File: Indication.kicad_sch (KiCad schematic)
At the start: 29 parts

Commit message: Убрал питание 3.3В
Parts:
- removed C10, C11, C12, C13, C14, C9: 56p, Capacitor_SMD:C_0805_2012Metric_Pad1.18x1.45mm_HandSolder, symbol Device:C_Small
- removed D11: FLT, LED_SMD:LED_0805_2012Metric_Pad1.15x1.40mm_HandSolder, symbol Device:LED_Small
- removed D12: RDY, LED_SMD:LED_0805_2012Metric_Pad1.15x1.40mm_HandSolder, symbol Device:LED_Small
- removed D13: SN74AC08DR, Package_SO:SOIC-14_3.9x8.7mm_P1.27mm, symbol Logic:SN74AC08DR
- removed R15: 10k, Resistor_SMD:R_0805_2012Metric_Pad1.20x1.40mm_HandSolder, symbol Device:R_Small
- removed R16, R18: 330, Resistor_SMD:R_0805_2012Metric_Pad1.20x1.40mm_HandSolder, symbol Device:R_Small
- removed R17, R19, R20, R21, R22: 120, Resistor_SMD:R_0805_2012Metric_Pad1.20x1.40mm_HandSolder, symbol Device:R_Small
- added D6: SN74AHC1G08DBVR, symbol Logic_My:SN74AHC1G08DBVR
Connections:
- net FLT_L1 is gone; now on net FLT: C7.1, D9.1 (K), R13.1
- net RDY_L1 is gone; now on net RDY: C8.1, R12.2, R14.1
- net FLT: now also D6.2 (A)
- net GND: now also D6.3 (GND)
- net RDY: now also D6.1 (B)
- net at D14.4 (DI): now also D6.4 (Y)
- net +3V3 renamed +5V
- net +5V: now also D6.5 (Vcc); no longer R13.2
- no-connect marks 4 -> 1
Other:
- moved on the sheet: C15

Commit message: Развел все дорожки
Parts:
- D6: footprint (none) -> Package_TO_SOT_SMD:SOT-23-5
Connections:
- net +5V: now also R13.2
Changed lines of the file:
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@@
-	)
-	(junction
-		(at 76.962 83.566)
-		(diameter 0)
-		(color 0 0 0 0)
 	)
 	(junction
@@
 		(color 0 0 0 0)
 	)
+	(junction
+		(at 76.835 83.82)
+		(diameter 0)
+		(color 0 0 0 0)
+	)
 	(no_connect
 		(at 221.996 95.758)
@@
 	(wire
 		(pts
+			(xy 76.835 83.185) (xy 76.835 83.82)
+		)
+		(stroke
+			(width 0)
+			(type default)
+		)
+	)
+	(wire
+		(pts
 			(xy 242.57 105.41) (xy 242.57 106.426)
 		)
@@
 	(wire
 		(pts
-			(xy 70.104 83.566) (xy 76.962 83.566)
+			(xy 69.977 83.82) (xy 76.835 83.82)
 		)
 		(stroke
@@
 	(wire
 		(pts
-			(xy 76.962 84.582) (xy 76.962 83.566)
+			(xy 76.835 84.836) (xy 76.835 83.82)
 		)
 		(stroke
@@
 	(global_label "FLT"
 		(shape input)
-		(at 70.104 83.566 180)
+		(at 69.977 83.82 180)
 		(fields_autoplaced yes)
 		(effects
@@
 		)
 		(property "Intersheetrefs" "${INTERSHEET_REFS}"
-			(at 64.0345 83.566 0)
+			(at 63.9075 83.82 0)
 			(effects
 				(font
@@
 	(symbol
 		(lib_id "power:+5V")
-		(at 76.962 78.232 0)
+		(at 76.835 78.105 0)
 		(unit 1)
 		(exclude_from_sim no)
@@
 		(dnp no)
 		(property "Reference" "#PWR017"
-			(at 76.962 82.042 0)
+			(at 76.835 81.915 0)
 			(effects
 				(font
@@
 		)
 		(property "Value" "+5V"
-			(at 76.962 74.676 0)
+			(at 76.835 74.549 0)
 			(effects
 				(font
@@
 		)
 		(property "Footprint" ""
-			(at 76.962 78.232 0)
+			(at 76.835 78.105 0)
 			(effects
 				(font
@@
 		)
 		(property "Datasheet" ""
-			(at 76.962 78.232 0)
+			(at 76.835 78.105 0)
 			(effects
 				(font
@@
 		)
 		(property "Description" "Power symbol creates a global label with name \"+5V\""
-			(at 76.962 78.232 0)
+			(at 76.835 78.105 0)
 			(effects
 				(font
@@
 			)
 		)
-		(property "Footprint" ""
+		(property "Footprint" "Package_TO_SOT_SMD:SOT-23-5"
 			(at 177.292 99.06 0)
 			(effects
@@
 	(symbol
 		(lib_id "power:GND")
-		(at 76.962 89.662 0)
+		(at 76.835 89.916 0)
 		(unit 1)
 		(exclude_from_sim no)
@@
 		(dnp no)
 		(property "Reference" "#PWR018"
-			(at 76.962 96.012 0)
+			(at 76.835 96.266 0)
 			(effects
 				(font
@@
 		)
 		(property "Value" "GND"
-			(at 74.93 93.726 0)
+			(at 74.803 93.98 0)
 			(effects
 				(font
@@
 		)
 		(property "Footprint" ""
-			(at 76.962 89.662 0)
+			(at 76.835 89.916 0)
 			(effects
 				(font
@@
 		)
 		(property "Datasheet" ""
-			(at 76.962 89.662 0)
+			(at 76.835 89.916 0)
 			(effects
 				(font
@@
 		)
 		(property "Description" ""
-			(at 76.962 89.662 0)
+			(at 76.835 89.916 0)
 			(effects
 				(font
@@
 	(symbol
 		(lib_id "Device:C_Small")
-		(at 76.962 87.122 0)
+		(at 76.835 87.376 0)
 		(unit 1)
 		(exclude_from_sim no)
@@
 		(dnp no)
 		(property "Reference" "C7"
-			(at 74.295 85.598 0)
+			(at 74.168 85.852 0)
 			(effects
 				(font
@@
 		)
 		(property "Value" "56p"
-			(at 73.279 88.773 0)
+			(at 73.152 89.027 0)
 			(effects
 				(font
@@
 		)
 		(property "Footprint" "Capacitor_SMD:C_0805_2012Metric_Pad1.18x1.45mm_HandSolder"
-			(at 76.962 87.122 0)
+			(at 76.835 87.376 0)
 			(effects
 				(font
@@
 		)
 		(property "Datasheet" "~"
-			(at 76.962 87.122 0)
+			(at 76.835 87.376 0)
 			(effects
 				(font
@@
 		)
 		(property "Description" ""
-			(at 76.962 87.122 0)
+			(at 76.835 87.376 0)
 			(effects
 				(font
@@
 	(symbol
 		(lib_id "Device:R_Small")
-		(at 76.962 81.026 180)
+		(at 76.835 80.645 180)
 		(unit 1)
 		(exclude_from_sim no)
@@
 		(dnp no)
 		(property "Reference" "R13"
-			(at 79.883 82.169 0)
+			(at 79.756 81.788 0)
 			(effects
 				(font
@@
 		)
 		(property "Value" "10k"
-			(at 79.883 80.391 0)
+			(at 79.756 80.01 0)
 			(effects
 				(font
@@
 		)
 		(property "Footprint" "Resistor_SMD:R_0805_2012Metric_Pad1.20x1.40mm_HandSolder"
-			(at 76.962 81.026 0)
+			(at 76.835 80.645 0)
 			(effects
 				(font
@@
 		)
 		(property "Datasheet" "~"
-			(at 76.962 81.026 0)
+			(at 76.835 80.645 0)
 			(effects
 				(font
@@
 		)
 		(property "Description" ""
-			(at 76.962 81.026 0)
-			(effects
-				(font
+			(at 76.835 80.645 0)
+			(effects
+				(font

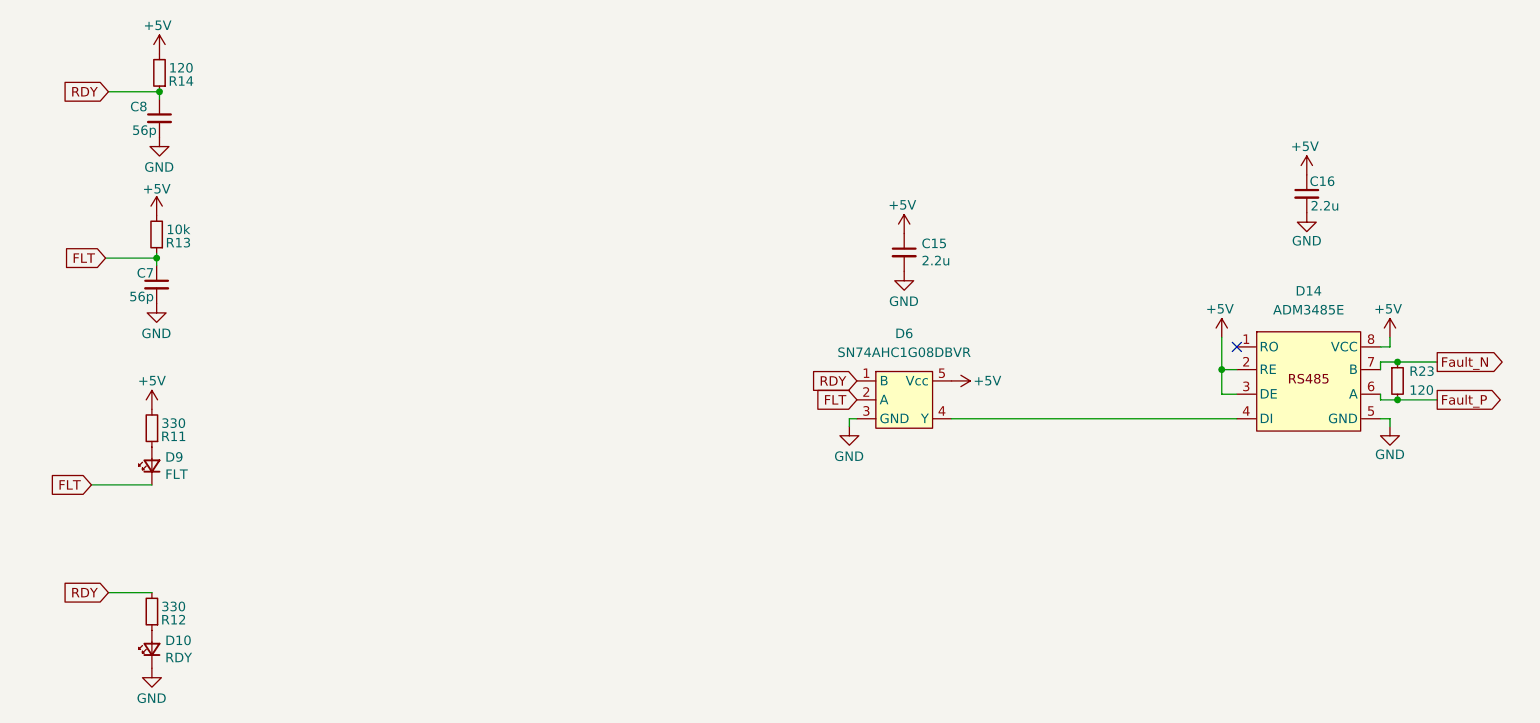
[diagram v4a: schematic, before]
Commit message: Изменения: изменил BOM, сделал заказ
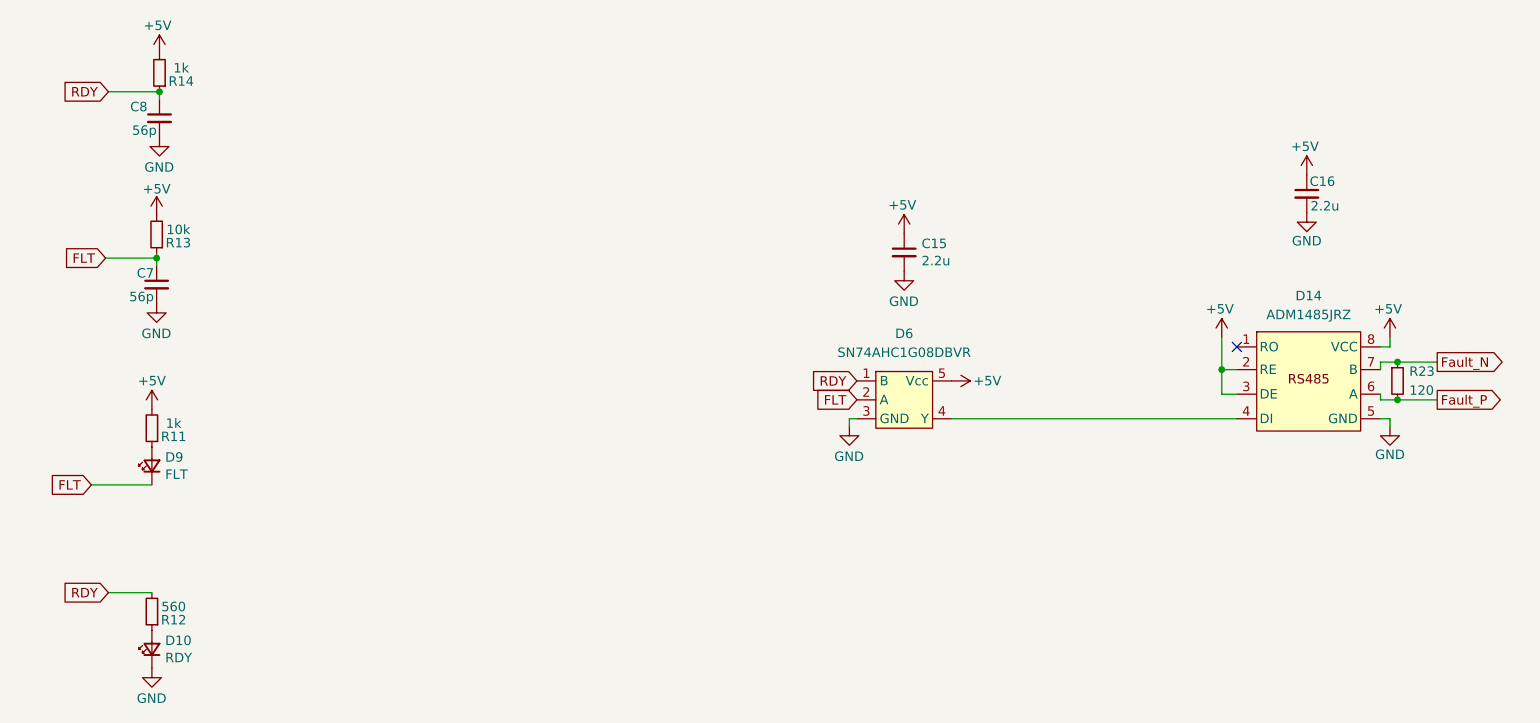
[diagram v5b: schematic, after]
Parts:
- D14: value ADM3485E -> ADM1485JRZ
- R11: value 330 -> 1k
- R12: value 330 -> 560
- R14: value 120 -> 1k
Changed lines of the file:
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@@
 			)
 		)
-		(property "Value" "120"
+		(property "Value" "1k"
 			(at 80.137 58.293 0)
 			(effects
@@
 		(fields_autoplaced yes)
 		(property "Reference" "D14"
-			(at 231.648 88.265 0)
-			(effects
-				(font
-					(size 1.27 1.27)
-				)
-			)
-		)
-		(property "Value" "ADM3485E"
-			(at 231.648 90.805 0)
+			(at 231.648 88.9 0)
+			(effects
+				(font
+					(size 1.27 1.27)
+				)
+			)
+		)
+		(property "Value" "ADM1485JRZ"
+			(at 231.648 91.44 0)
 			(effects
 				(font
@@
 			)
 		)
-		(property "Value" "330"
+		(property "Value" "560"
 			(at 79.121 130.683 0)
 			(effects
@@
 			)
 		)
-		(property "Value" "330"
+		(property "Value" "1k"
 			(at 79.121 106.045 0)
 			(effects

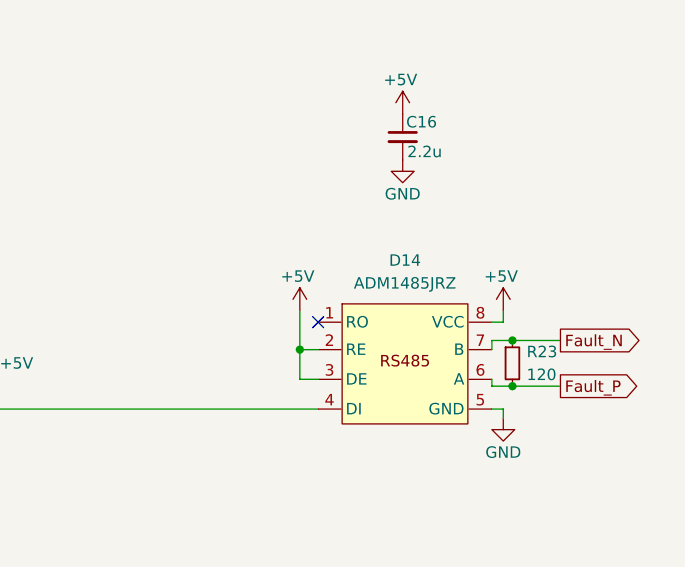
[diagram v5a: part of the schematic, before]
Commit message: VER2_Test: добавил новый BOM и в схеме заменил названия компонентов
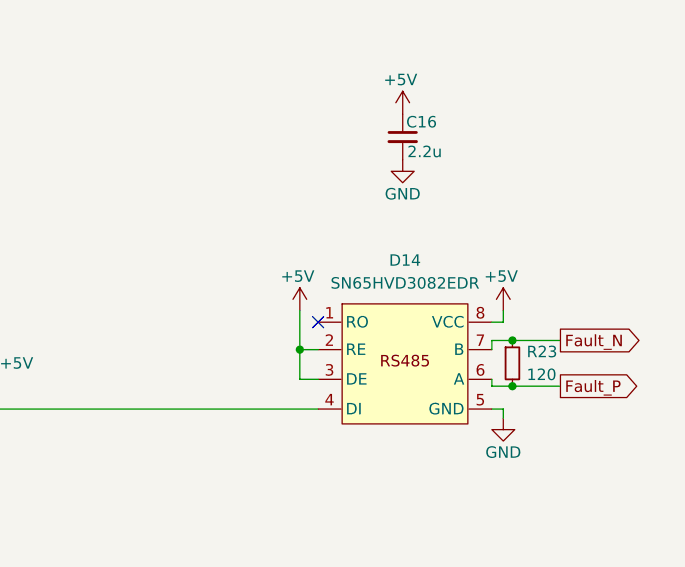
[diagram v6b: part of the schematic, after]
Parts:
- D14: value ADM1485JRZ -> SN65HVD3082EDR
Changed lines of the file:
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@@
 			)
 		)
-		(property "Value" "ADM1485JRZ"
+		(property "Value" "SN65HVD3082EDR"
 			(at 231.648 91.44 0)
 			(effects
